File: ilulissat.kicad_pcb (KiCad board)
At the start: 2 copper layers, 25.4 x 25.4 mm, 29 parts, among them SW1 SW_SPST, U1 EFR32MG21x, U2 HDC2080, Y1 32.768Khz, Y2 38.4Mhz

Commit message: Add a user button
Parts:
- removed TP101: SWDIO, TestPoint:TestPoint_Pad_D1.0mm
- removed TP102: SWCLK, TestPoint:TestPoint_Pad_D1.0mm
- added J1: Conn_01x04, Connector_PinHeader_1.27mm:PinHeader_1x04_P1.27mm_Vertical, F.Cu at (156.3, 91.1)
- added SW2: USR, Button_Switch_SMD:SW_SPST_B3U-1000P, F.Cu at (153.7, 105.8)
- SW1: value SW_SPST -> ~RST~
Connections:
- U1 pad 4: Net-(U1-Pad4) -> /~USRBTN~
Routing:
- net /~USRBTN~: track 0.00 -> 17.2 mm
- net VDD: track 73.6 -> 79.5 mm
- net /SWCLK: track 8.93 -> 12.2 mm
- net /SWDIO: track 8.19 -> 10.6 mm
- net /~RESET~: track 11.6 -> 13.0 mm

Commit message: Fun tests
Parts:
- moved SW1 3.40 mm to (153.7, 105.8)
- moved SW2 3.40 mm to (153.7, 109.2)
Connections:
- U1 pad 23: Net-(U1-Pad23) -> /HDC_INT
- U1 pad 3: /HDC_INT -> Net-(U1-Pad3)
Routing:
- net /HDC_INT: track 16.3 -> 29.0 mm, vias 0 -> 2
- net /~RESET~: track 13.0 -> 8.57 mm
- net GND: vias 52 -> 63

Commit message: Finished?
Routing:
- net /HDC_INT: track 29.0 -> 29.8 mm
- net GND: vias 63 -> 62
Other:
- board text added: "+"

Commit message: Align some text
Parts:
- SW1: value ~RST~ -> RST
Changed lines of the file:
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@@
       (effects (font (size 1 1) (thickness 0.15)))
     )
-    (fp_text value USR (at 4 0.6) (layer F.SilkS)
+    (fp_text value USR (at 3.275 -0.6 90) (layer F.SilkS)
       (effects (font (size 1 1) (thickness 0.15)))
     )
@@
       (effects (font (size 1 1) (thickness 0.15)))
     )
-    (fp_text value ~RST~ (at 3.9 -0.7) (layer F.SilkS)
-      (effects (font (size 1 1) (thickness 0.15)))
-    )
+    (fp_text value RST (at 3.275 -0.575 90) (layer F.SilkS)
+      (effects (font (size 1 1) (thickness 0.15)))
+    )

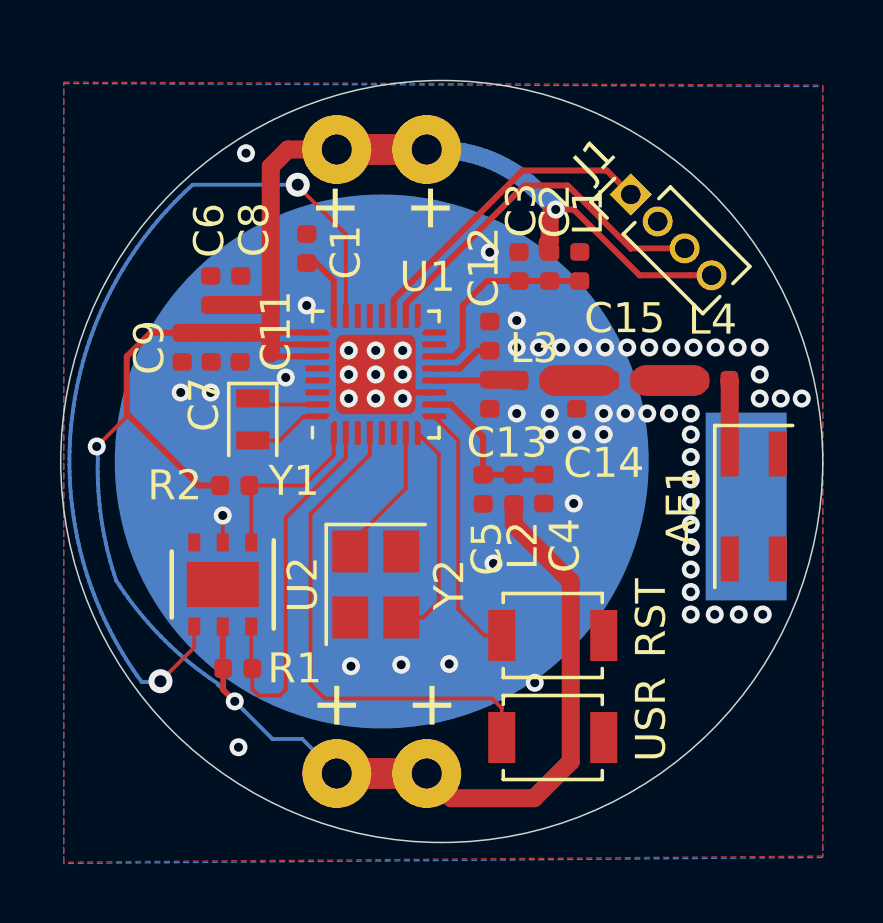
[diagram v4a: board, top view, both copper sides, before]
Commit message: Add UART
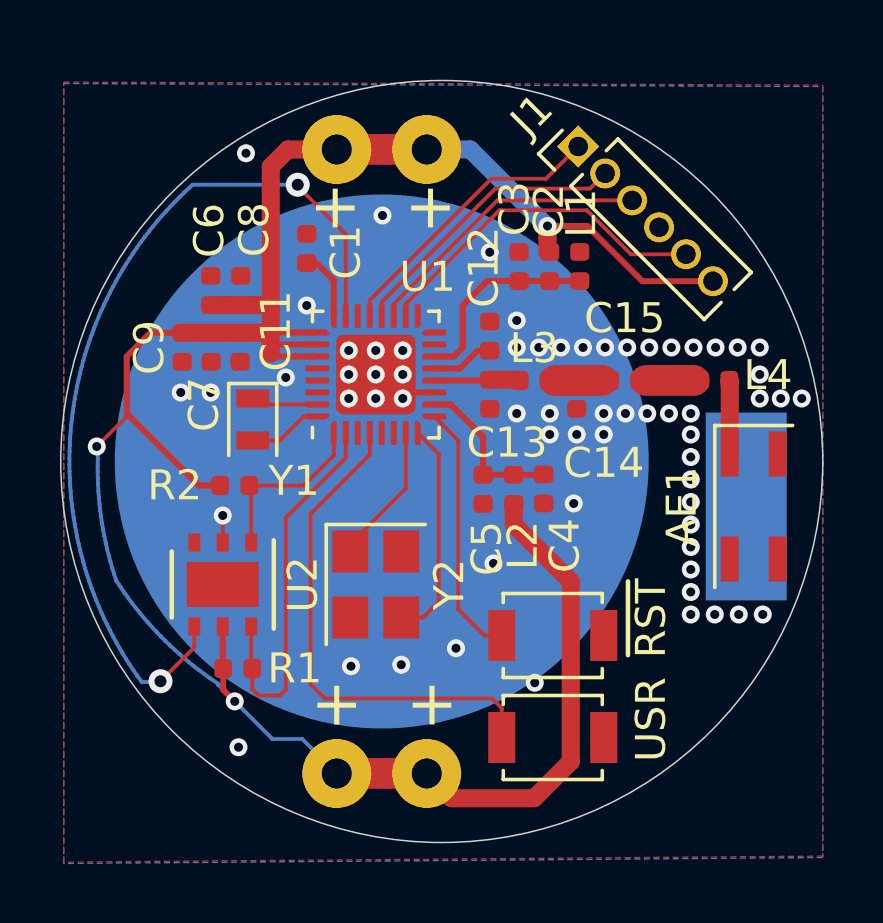
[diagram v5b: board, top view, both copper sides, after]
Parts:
- J1: value Conn_01x04 -> Conn_01x06; footprint Connector_PinHeader_1.27mm:PinHeader_1x04_P1.27mm_Vertical -> Connector_PinHeader_1.27mm:PinHeader_1x06_P1.27mm_Vertical
- SW1: value RST -> ~RST~
- moved J1 2.37 mm to (154.6, 89.5)
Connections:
- J1 pad 1: /SWDIO -> /UART_TX
- J1 pad 2: GND -> /UART_RX
- J1 pad 3: /SWCLK -> /SWDIO
- J1 pad 4: VDD -> GND
- U1 pad 20: Net-(U1-Pad20) -> /UART_RX
- U1 pad 21: Net-(U1-Pad21) -> /UART_TX
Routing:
- net /UART_RX: track 0.00 -> 9.69 mm
- net /UART_TX: track 0.00 -> 9.60 mm
- net /SWDIO: track 10.6 -> 9.78 mm
- net /SWCLK: track 12.2 -> 11.6 mm
- net GND: vias 62 -> 63

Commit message: Add LED
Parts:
- added D1: RED, LED_SMD:LED_0402_1005Metric, F.Cu at (148.9, 107.8)
- added R3: 360R, Resistor_SMD:R_0402_1005Metric, F.Cu at (147.0, 107.8)
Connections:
- U1 pad 3: Net-(U1-Pad3) -> /USRLED
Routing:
- net /USRLED: track 0.00 -> 10.0 mm
- net Net-(D1-Pad2): track 0.00 -> 0.96 mm
- net VDD: track 78.6 -> 79.5 mm
- net /~USRBTN~: track 16.9 -> 16.1 mm
- net GND: vias 63 -> 61

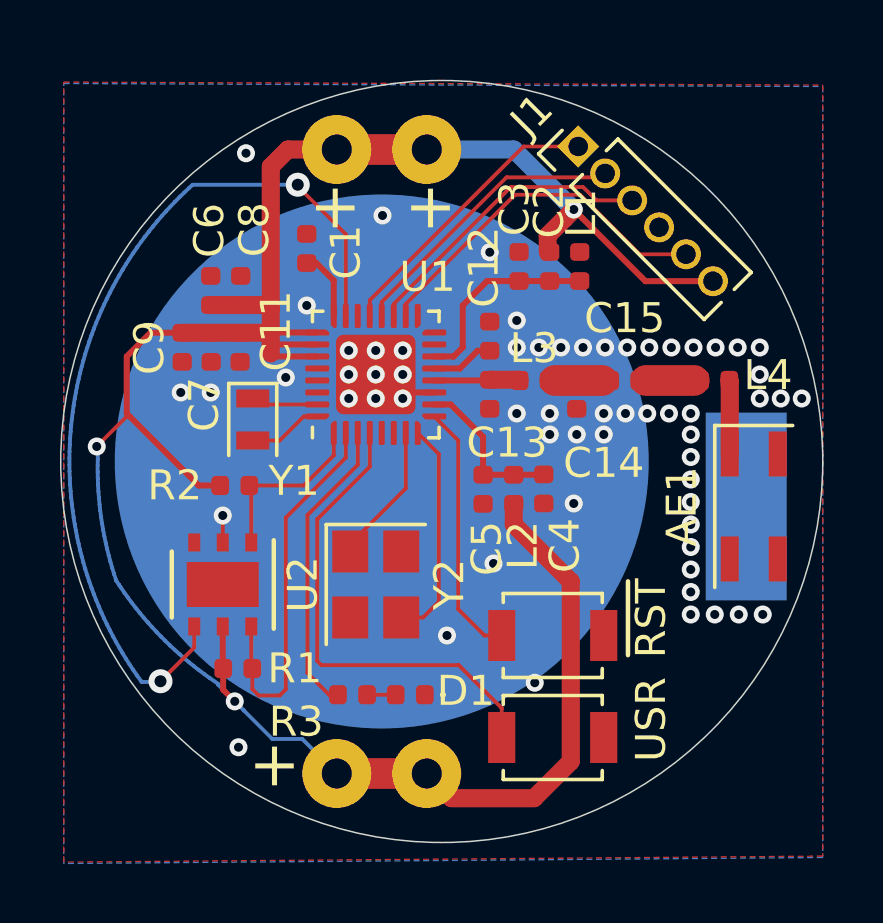
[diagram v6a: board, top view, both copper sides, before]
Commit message: Make DRC unhappy for less risk of shorts
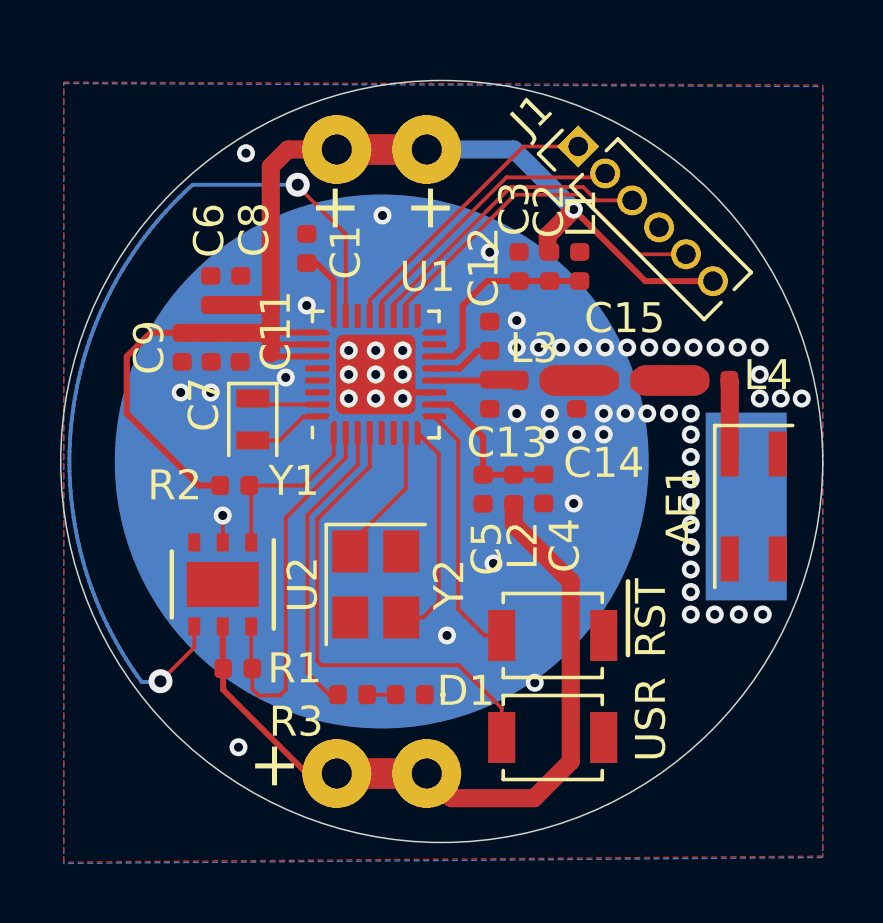
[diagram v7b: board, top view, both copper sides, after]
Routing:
- net VDD: track 79.5 -> 67.8 mm, vias 3 -> 1
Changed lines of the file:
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@@
     (thickness 1.6)
     (drawings 4)
-    (tracks 348)
+    (tracks 290)
     (zones 0)
     (modules 31)
@@
   )
   (setup
-    (last_trace_width 0.127)
+    (last_trace_width 0.2)
     (user_trace_width 0.127)
     (user_trace_width 0.2)
@@
   (segment (start 146.4 93.965) (end 145.82 93.385) (width 0.2) (layer F.Cu) (net 2))
   (segment (start 146.4 95.15) (end 146.4 93.965) (width 0.2) (layer F.Cu) (net 2))
-  (segment (start 142.544379 107.410379) (end 142.551028 107.447017) (width 0.127) (layer B.Cu) (net 3))
-  (segment (start 142.257049 107.211326) (end 142.544379 107.410379) (width 0.127) (layer B.Cu) (net 3))
   (segment (start 149.5 89.6) (end 146.5 89.6) (width 1.026) (layer F.Cu) (net 3))
-  (segment (start 146.5 110.4) (end 145.350001 109.250001) (width 0.127) (layer B.Cu) (net 3))
-  (segment (start 139.540705 104.538985) (end 139.667743 104.709528) (width 0.127) (layer B.Cu) (net 3))
-  (segment (start 139.416798 104.366225) (end 139.540705 104.538985) (width 0.127) (layer B.Cu) (net 3))
-  (segment (start 138.555804 100.998212) (end 138.572315 101.213704) (width 0.127) (layer B.Cu) (net 3))
-  (segment (start 138.592809 101.428867) (end 138.617282 101.64365) (width 0.127) (layer B.Cu) (net 3))
-  (segment (start 138.5 99.5) (end 138.491897 99.508102) (width 0.127) (layer B.Cu) (net 3))
-  (segment (start 138.617282 101.64365) (end 138.645707 101.857826) (width 0.127) (layer B.Cu) (net 3))
-  (segment (start 139.145388 103.957382) (end 139.150513 103.972089) (width 0.127) (layer B.Cu) (net 3))
   (segment (start 154.3 110) (end 154.3 104) (width 0.6) (layer F.Cu) (net 3))
-  (segment (start 144.354012 109.250001) (end 143.399999 108.295988) (width 0.127) (layer B.Cu) (net 3))
   (segment (start 144.185 94.785) (end 142.3 94.785) (width 0.6) (layer F.Cu) (net 3))
   (segment (start 142.615 100.8) (end 141.9 100.8) (width 0.2) (layer F.Cu) (net 3))
-  (segment (start 142.715 107.610989) (end 143.1 107.995989) (width 0.2) (layer F.Cu) (net 3))
-  (segment (start 142.715 106.9) (end 142.715 107.610989) (width 0.2) (layer F.Cu) (net 3))
-  (segment (start 138.491897 99.508102) (end 138.545295 99.565314) (width 0.127) (layer B.Cu) (net 3))
-  (segment (start 141.256795 106.420506) (end 141.417442 106.559735) (width 0.127) (layer B.Cu) (net 3))
-  (segment (start 139.7978 104.877706) (end 139.930894 105.043539) (width 0.127) (layer B.Cu) (net 3))
-  (segment (start 138.533123 99.918236) (end 138.529668 100.134362) (width 0.127) (layer B.Cu) (net 3))
-  (segment (start 138.529668 100.134362) (end 138.53021 100.350395) (width 0.127) (layer B.Cu) (net 3))
-  (segment (start 140.347793 105.526235) (end 140.492453 105.681995) (width 0.127) (layer B.Cu) (net 3))
-  (segment (start 138.714431 102.284545) (end 138.754704 102.496904) (width 0.127) (layer B.Cu) (net 3))
   (segment (start 144.3 94.9) (end 144.185 94.785) (width 0.6) (layer F.Cu) (net 3))
-  (segment (start 139.014526 103.545474) (end 139.078066 103.752074) (width 0.127) (layer B.Cu) (net 3))
   (segment (start 146.5 89.6) (end 144.873655 89.6) (width 0.6) (layer F.Cu) (net 3))
   (segment (start 144.873655 89.6) (end 144.3 90.173655) (width 0.6) (layer F.Cu) (net 3))
   (segment (start 150.325 111.225) (end 153.075 111.225) (width 0.6) (layer F.Cu) (net 3))
-  (via (at 138.5 99.5) (size 0.6) (drill 0.3) (layers F.Cu B.Cu) (net 3))
   (segment (start 139.6 98.5) (end 139.5 98.4) (width 0.2) (layer F.Cu) (net 3))
   (segment (start 139.5 98.4) (end 139.5 96.5) (width 0.2) (layer F.Cu) (net 3))
   (segment (start 142.7 105.5) (end 142.7 106.885) (width 0.2) (layer F.Cu) (net 3))
-  (segment (start 138.5 99.5) (end 139.5 98.5) (width 0.127) (layer F.Cu) (net 3))
   (segment (start 144.3 90.173655) (end 144.3 94.9) (width 0.6) (layer F.Cu) (net 3))
   (segment (start 149.5 110.4) (end 146.5 110.4) (width 1.026) (layer F.Cu) (net 3))
   (segment (start 142.7 106.885) (end 142.715 106.9) (width 0.2) (layer F.Cu) (net 3))
   (segment (start 141.9 100.8) (end 139.6 98.5) (width 0.2) (layer F.Cu) (net 3))
-  (segment (start 139.5 98.5) (end 139.6 98.5) (width 0.127) (layer F.Cu) (net 3))
   (segment (start 145.85 96.1) (end 144.3 96.1) (width 0.2) (layer F.Cu) (net 3))
   (segment (start 140.291 95.709) (end 141.348 95.709) (width 0.2) (layer F.Cu) (net 3))
   (segment (start 139.5 96.5) (end 140.291 95.709) (width 0.2) (layer F.Cu) (net 3))
   (segment (start 152.4 102.1) (end 152.4 101.4125) (width 0.6) (layer F.Cu) (net 3))
-  (via (at 143.1 107.995989) (size 0.6) (drill 0.3) (layers F.Cu B.Cu) (net 3))
-  (segment (start 145.350001 109.250001) (end 144.354012 109.250001) (width 0.127) (layer B.Cu) (net 3))
   (segment (start 144.291 95.709) (end 141.348 95.709) (width 0.6) (layer F.Cu) (net 3))
   (segment (start 145.85 96.5) (end 144.4 96.5) (width 0.2) (layer F.Cu) (net 3))
-  (segment (start 138.53021 100.350395) (end 138.534748 100.566497) (width 0.127) (layer B.Cu) (net 3))
-  (segment (start 138.543279 100.782441) (end 138.555804 100.998212) (width 0.127) (layer B.Cu) (net 3))
-  (segment (start 139.312137 104.214596) (end 139.416798 104.366225) (width 0.127) (layer B.Cu) (net 3))
-  (segment (start 138.798901 102.708502) (end 138.846992 102.919196) (width 0.127) (layer B.Cu) (net 3))
-  (segment (start 139.150513 103.972089) (end 139.25198 104.124914) (width 0.127) (layer B.Cu) (net 3))
-  (segment (start 141.098643 106.278366) (end 141.256795 106.420506) (width 0.127) (layer B.Cu) (net 3))
-  (segment (start 138.846992 102.919196) (end 138.898983 103.129016) (width 0.127) (layer B.Cu) (net 3))
   (segment (start 144.3 95.7) (end 144.3 96.1) (width 0.6) (layer F.Cu) (net 3))
   (segment (start 144.3 94.9) (end 144.3 95.7) (width 0.6) (layer F.Cu) (net 3))
-  (segment (start 138.572315 101.213704) (end 138.592809 101.428867) (width 0.127) (layer B.Cu) (net 3))
-  (segment (start 141.914193 106.959809) (end 142.084524 107.087141) (width 0.127) (layer B.Cu) (net 3))
-  (segment (start 138.954826 103.337768) (end 139.014526 103.545474) (width 0.127) (layer B.Cu) (net 3))
-  (segment (start 139.078066 103.752074) (end 139.145388 103.957382) (width 0.127) (layer B.Cu) (net 3))
-  (segment (start 139.252689 104.125058) (end 139.312137 104.214596) (width 0.127) (layer B.Cu) (net 3))
-  (segment (start 138.534748 100.566497) (end 138.543279 100.782441) (width 0.127) (layer B.Cu) (net 3))
-  (segment (start 139.25198 104.124914) (end 139.252689 104.125058) (width 0.127) (layer B.Cu) (net 3))
   (segment (start 154.3 104) (end 152.4 102.1) (width 0.6) (layer F.Cu) (net 3))
   (segment (start 144.4 96.5) (end 144.3 96.4) (width 0.2) (layer F.Cu) (net 3))
   (segment (start 144.3 95.7) (end 144.291 95.709) (width 0.6) (layer F.Cu) (net 3))
-  (segment (start 140.492453 105.681995) (end 140.639971 105.835196) (width 0.127) (layer B.Cu) (net 3))
-  (segment (start 138.754704 102.496904) (end 138.798901 102.708502) (width 0.127) (layer B.Cu) (net 3))
-  (segment (start 138.645707 101.857826) (end 138.678109 102.071583) (width 0.127) (layer B.Cu) (net 3))
   (segment (start 149.5 110.4) (end 150.325 111.225) (width 0.6) (layer F.Cu) (net 3))
-  (segment (start 140.066969 105.206958) (end 140.205944 105.367866) (width 0.127) (layer B.Cu) (net 3))
-  (segment (start 142.084524 107.087141) (end 142.257049 107.211326) (width 0.127) (layer B.Cu) (net 3))
-  (segment (start 141.417442 106.559735) (end 141.422333 106.563822) (width 0.127) (layer B.Cu) (net 3))
-  (segment (start 139.930894 105.043539) (end 140.066969 105.206958) (width 0.127) (layer B.Cu) (net 3))
-  (segment (start 142.800001 107.69599) (end 143.1 107.995989) (width 0.127) (layer B.Cu) (net 3))
-  (segment (start 139.667743 104.709528) (end 139.7978 104.877706) (width 0.127) (layer B.Cu) (net 3))
-  (segment (start 138.545295 99.565314) (end 138.533123 99.918236) (width 0.127) (layer B.Cu) (net 3))
-  (segment (start 143.399999 108.295988) (end 143.1 107.995989) (width 0.127) (layer B.Cu) (net 3))
   (segment (start 144.3 96.1) (end 144.3 96.4) (width 0.6) (layer F.Cu) (net 3))
-  (segment (start 138.898983 103.129016) (end 138.954826 103.337768) (width 0.127) (layer B.Cu) (net 3))
-  (segment (start 138.678109 102.071583) (end 138.714431 102.284545) (width 0.127) (layer B.Cu) (net 3))
-  (segment (start 142.551028 107.447017) (end 142.800001 107.69599) (width 0.127) (layer B.Cu) (net 3))
-  (segment (start 141.746195 106.829431) (end 141.914193 106.959809) (width 0.127) (layer B.Cu) (net 3))
-  (segment (start 140.943123 106.133435) (end 141.098643 106.278366) (width 0.127) (layer B.Cu) (net 3))
-  (segment (start 140.790171 105.985651) (end 140.943123 106.133435) (width 0.127) (layer B.Cu) (net 3))
-  (segment (start 140.639971 105.835196) (end 140.790171 105.985651) (width 0.127) (layer B.Cu) (net 3))
-  (segment (start 141.580601 106.696065) (end 141.746195 106.829431) (width 0.127) (layer B.Cu) (net 3))
-  (segment (start 140.205944 105.367866) (end 140.347793 105.526235) (width 0.127) (layer B.Cu) (net 3))
-  (segment (start 141.422333 106.563822) (end 141.580601 106.696065) (width 0.127) (layer B.Cu) (net 3))
   (segment (start 145.85 95.7) (end 144.3 95.7) (width 0.2) (layer F.Cu) (net 3))
   (segment (start 153.075 111.225) (end 154.3 110) (width 0.6) (layer F.Cu) (net 3))
@@
   (segment (start 159.040128 93.990128) (end 156.790128 93.990128) (width 0.2) (layer F.Cu) (net 3))
   (segment (start 153.53049 93.015) (end 153.53049 92.46951) (width 0.6) (layer F.Cu) (net 3))
+  (segment (start 145.504011 110.4) (end 146.5 110.4) (width 0.2) (layer F.Cu) (net 3))
+  (segment (start 142.715 106.9) (end 142.715 107.610989) (width 0.2) (layer F.Cu) (net 3))
+  (segment (start 142.715 107.610989) (end 145.504011 110.4) (width 0.2) (layer F.Cu) (net 3))
   (segment (start 153.765 97.3) (end 155.35899 97.3) (width 1.026) (layer F.Cu) (net 4))
   (segment (start 155.15622 91.296051) (end 154.715656 90.855487) (width 0.127) (layer F.Cu) (net 8))

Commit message: Rev1
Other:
- net class Default: clearance 0.2 -> 0.127; trace_width 0.25 -> 0.2
- rule trace_clearance: 0.2 -> 0.127
